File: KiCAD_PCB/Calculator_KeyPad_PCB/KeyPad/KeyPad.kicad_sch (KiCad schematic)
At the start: 42 parts

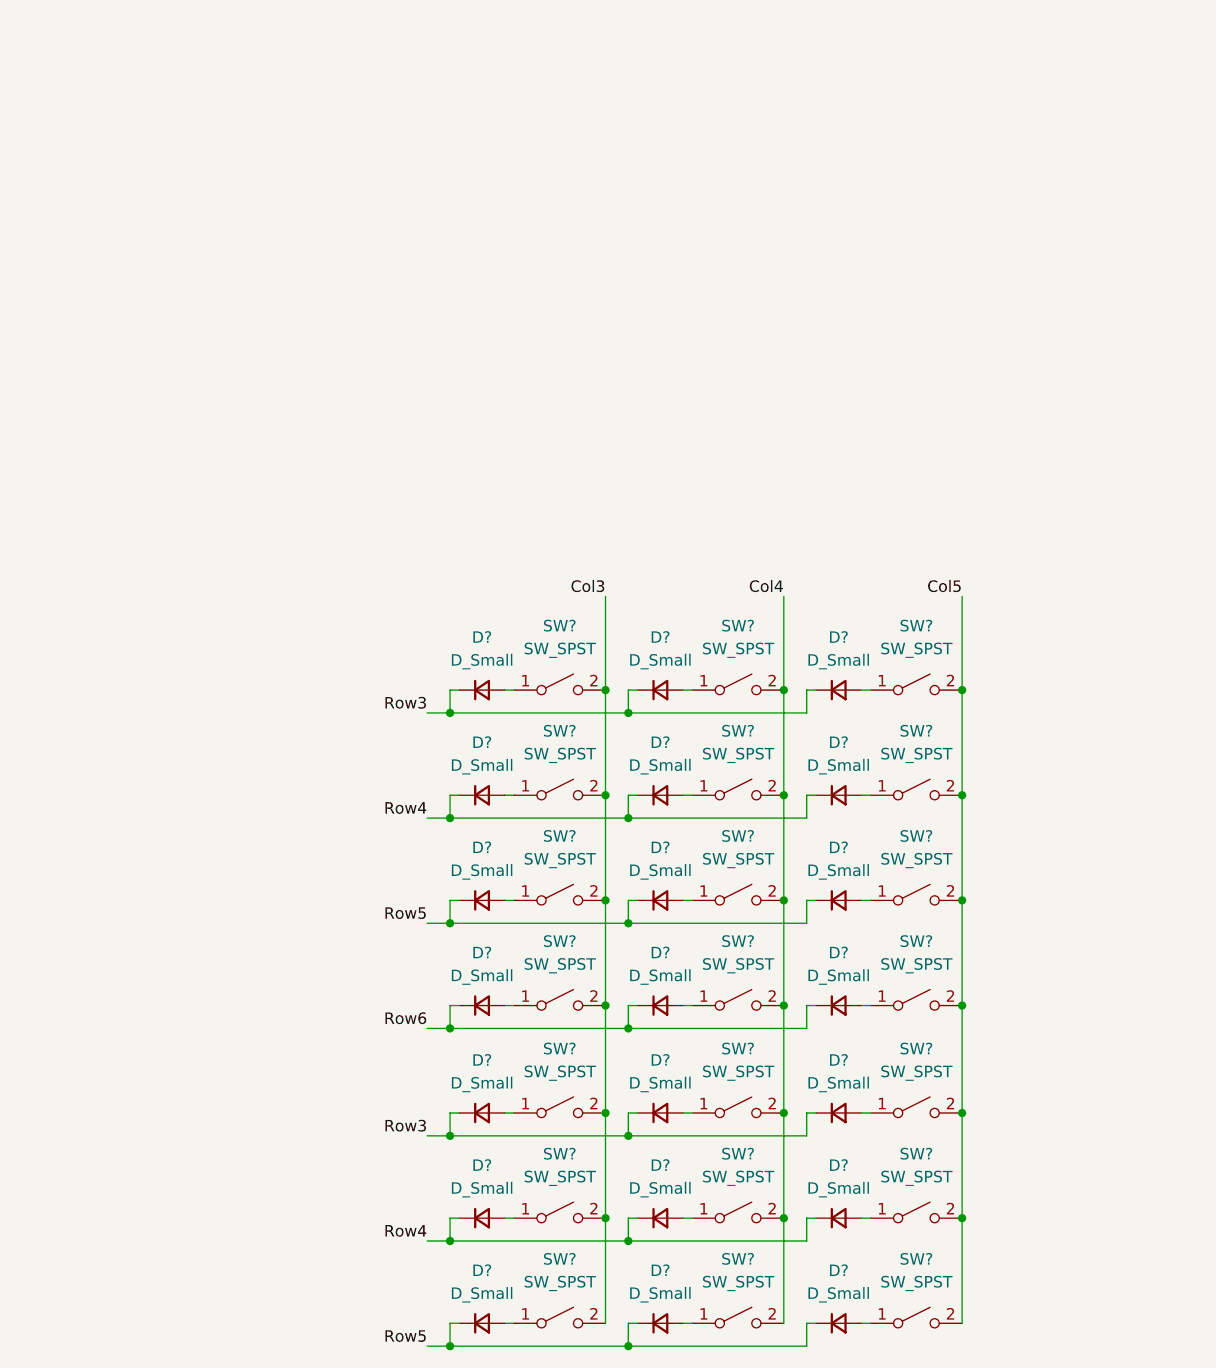
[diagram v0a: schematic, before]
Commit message: Updated NumberPad Schematic
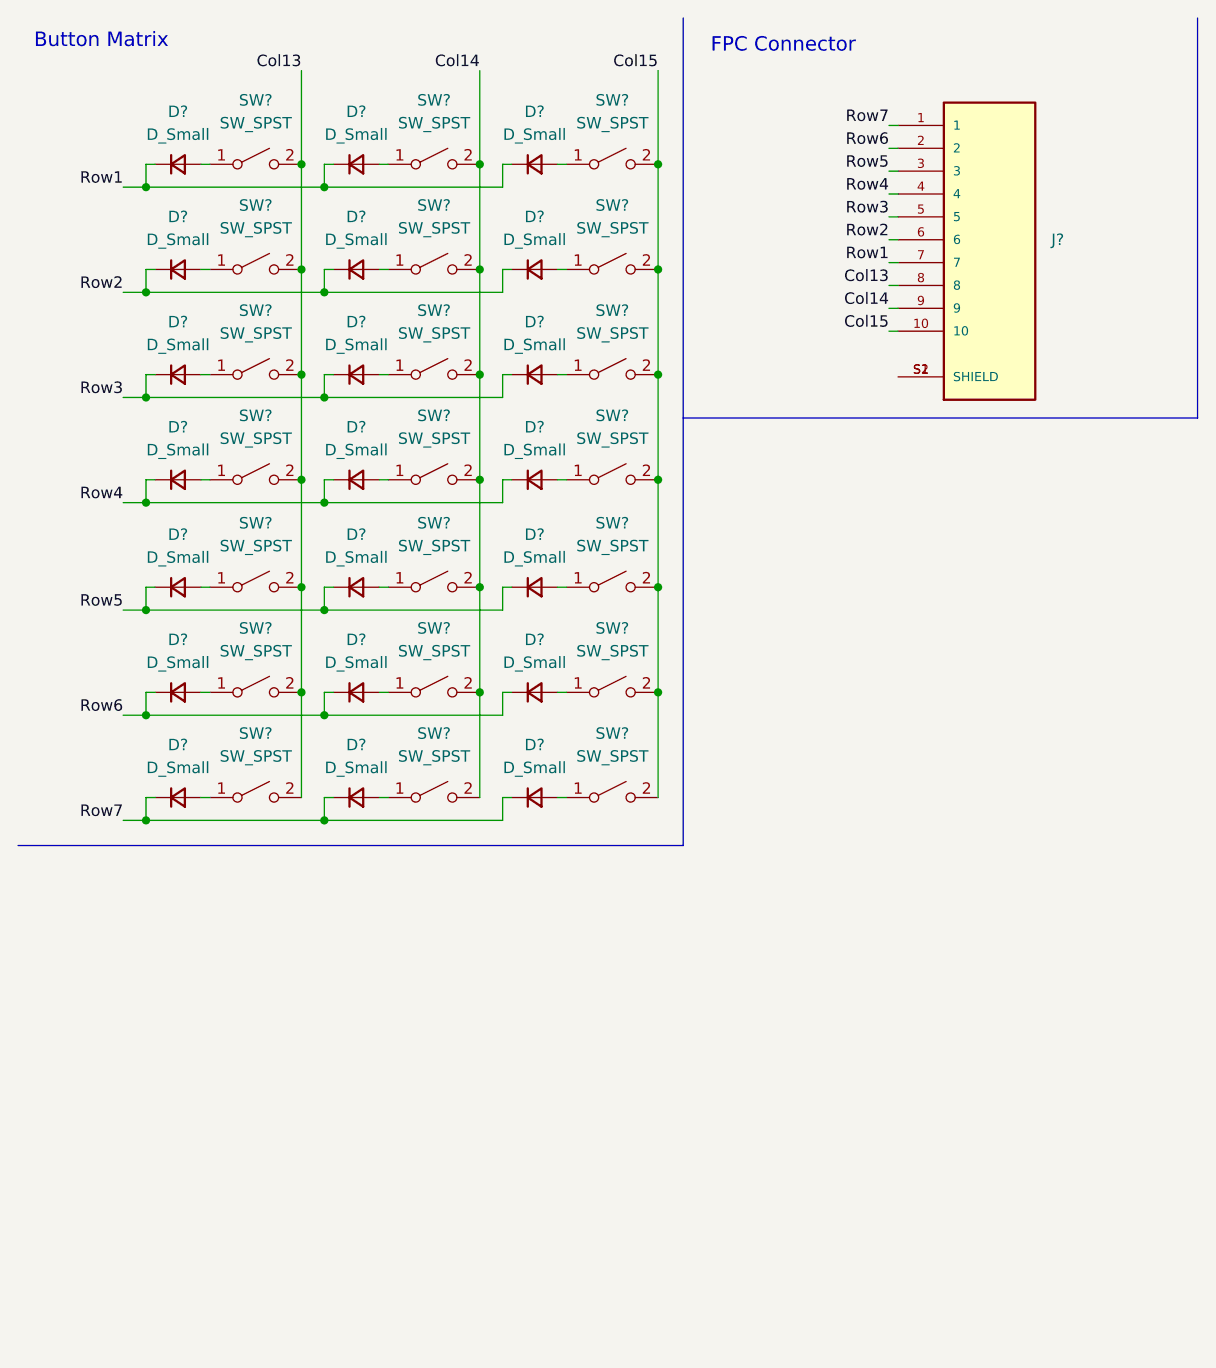
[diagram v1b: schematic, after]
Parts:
- added J?: (no value), symbol 5034801000:5034801000
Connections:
- net Row3: now also D?.1 (K), D?.1 (K), D?.1 (K), J?.5; no longer D?.1 (K), D?.1 (K), D?.1 (K), D?.1 (K), D?.1 (K), D?.1 (K)
- net Row4: now also D?.1 (K), D?.1 (K), D?.1 (K), J?.4; no longer D?.1 (K), D?.1 (K), D?.1 (K), D?.1 (K), D?.1 (K), D?.1 (K)
- net Row5: now also D?.1 (K), D?.1 (K), D?.1 (K), J?.3; no longer D?.1 (K), D?.1 (K), D?.1 (K), D?.1 (K), D?.1 (K), D?.1 (K)
- net Row6: now also D?.1 (K), D?.1 (K), D?.1 (K), J?.2; no longer D?.1 (K), D?.1 (K), D?.1 (K)
- net Col3 renamed Col13
- net Col13: now also J?.8
- net Col4 renamed Col14
- net Col14: now also J?.9
- net Col5 renamed Col15
- net Col15: now also J?.10
- new net: J?.S1 (SHIELD), J?.S2 (SHIELD)
- new net Row1: D?.1 (K), D?.1 (K), D?.1 (K), J?.7
- new net Row2: D?.1 (K), D?.1 (K), D?.1 (K), J?.6
- new net Row7: D?.1 (K), D?.1 (K), D?.1 (K), J?.1
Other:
- note added: "Button Matrix"
- note added: "FPC Connector"
- title: (none) -> Calculator Number Pad Module
- moved on the sheet: D?, SW?

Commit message: Finished NumPad Schematic
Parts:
- gave numbers to parts that had none: 43

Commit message: Working on PCB
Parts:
- SW1, SW10, SW11, SW12, SW13, SW14, SW15, SW16, SW17, SW18, SW19, SW2, SW20, SW21, SW3, SW4, SW5, SW6, SW7, SW8, SW9: footprint KSA1M331LFT_Footprint:KSA1M331LFT -> (none)

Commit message: NumPad Updates
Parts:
- J1: value (none) -> 5034801000; footprint (none) -> 5034801000:MOLEX_5034801000
- SW1, SW10, SW11, SW12, SW13, SW14, SW15, SW16, SW17, SW18, SW19, SW2, SW20, SW21, SW3, SW4, SW5, SW6, SW7, SW8, SW9: footprint (none) -> KSA_Switch:KSA1M331LFT
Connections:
- net Col13: now also J1.3; no longer J1.8
- net Col14: now also J1.2; no longer J1.9
- net Col15: now also J1.1; no longer J1.10
- net Row1: now also J1.4; no longer J1.7
- net Row2: now also J1.5; no longer J1.6
- net Row3: now also J1.6; no longer J1.5
- net Row4: now also J1.7; no longer J1.4
- net Row5: now also J1.8; no longer J1.3
- net Row6: now also J1.9; no longer J1.2
- net Row7: now also J1.10; no longer J1.1
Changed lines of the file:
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@@
     (effects (font (size 1.6 1.6)) (justify left bottom))
   )
-  (label "Row6" (at 108.712 26.67 180)
-    (effects (font (size 1.27 1.27)) (justify right bottom))
-  )
-  (label "Col13" (at 108.712 41.91 180)
+  (label "Row6" (at 108.712 44.45 180)
+    (effects (font (size 1.27 1.27)) (justify right bottom))
+  )
+  (label "Col13" (at 108.712 29.21 180)
     (effects (font (size 1.27 1.27)) (justify right bottom))
   )
@@
     (effects (font (size 1.27 1.27)) (justify right bottom))
   )
-  (label "Row4" (at 108.712 31.75 180)
-    (effects (font (size 1.27 1.27)) (justify right bottom))
-  )
-  (label "Row2" (at 108.712 36.83 180)
-    (effects (font (size 1.27 1.27)) (justify right bottom))
-  )
-  (label "Col15" (at 108.712 46.99 180)
+  (label "Row4" (at 108.712 39.37 180)
+    (effects (font (size 1.27 1.27)) (justify right bottom))
+  )
+  (label "Row2" (at 108.712 34.29 180)
+    (effects (font (size 1.27 1.27)) (justify right bottom))
+  )
+  (label "Col15" (at 108.712 24.13 180)
     (effects (font (size 1.27 1.27)) (justify right bottom))
   )
@@
     (effects (font (size 1.27 1.27)) (justify right bottom))
   )
-  (label "Row1" (at 108.712 39.37 180)
-    (effects (font (size 1.27 1.27)) (justify right bottom))
-  )
-  (label "Col14" (at 108.712 44.45 180)
+  (label "Row1" (at 108.712 31.75 180)
+    (effects (font (size 1.27 1.27)) (justify right bottom))
+  )
+  (label "Col14" (at 108.712 26.67 180)
     (effects (font (size 1.27 1.27)) (justify right bottom))
   )
@@
     (effects (font (size 1.27 1.27)) (justify right bottom))
   )
-  (label "Row3" (at 108.712 34.29 180)
-    (effects (font (size 1.27 1.27)) (justify right bottom))
-  )
-  (label "Row7" (at 108.712 24.13 180)
-    (effects (font (size 1.27 1.27)) (justify right bottom))
-  )
-  (label "Row5" (at 108.712 29.21 180)
+  (label "Row3" (at 108.712 36.83 180)
+    (effects (font (size 1.27 1.27)) (justify right bottom))
+  )
+  (label "Row7" (at 108.712 46.99 180)
+    (effects (font (size 1.27 1.27)) (justify right bottom))
+  )
+  (label "Row5" (at 108.712 41.91 180)
     (effects (font (size 1.27 1.27)) (justify right bottom))
   )
@@
     (property "Reference" "SW1" (id 0) (at 38.354 21.336 0))
     (property "Value" "SW_SPST" (id 1) (at 38.354 23.876 0))
-    (property "Footprint" "" (id 2) (at 38.354 28.448 0)
+    (property "Footprint" "KSA_Switch:KSA1M331LFT" (id 2) (at 38.354 28.448 0)
       (effects (font (size 1.27 1.27)) hide)
     )
@@
     (property "Reference" "SW5" (id 0) (at 38.354 68.326 0))
     (property "Value" "SW_SPST" (id 1) (at 38.354 70.866 0))
-    (property "Footprint" "" (id 2) (at 38.354 75.438 0)
+    (property "Footprint" "KSA_Switch:KSA1M331LFT" (id 2) (at 38.354 75.438 0)
       (effects (font (size 1.27 1.27)) hide)
     )
@@
     (property "Reference" "SW20" (id 0) (at 77.978 80.01 0))
     (property "Value" "SW_SPST" (id 1) (at 77.978 82.55 0))
-    (property "Footprint" "" (id 2) (at 77.978 87.122 0)
+    (property "Footprint" "KSA_Switch:KSA1M331LFT" (id 2) (at 77.978 87.122 0)
       (effects (font (size 1.27 1.27)) hide)
     )
@@
     (property "Reference" "SW6" (id 0) (at 38.354 80.01 0))
     (property "Value" "SW_SPST" (id 1) (at 38.354 82.55 0))
-    (property "Footprint" "" (id 2) (at 38.354 87.122 0)
+    (property "Footprint" "KSA_Switch:KSA1M331LFT" (id 2) (at 38.354 87.122 0)
       (effects (font (size 1.27 1.27)) hide)
     )
@@
     (property "Reference" "SW2" (id 0) (at 38.354 33.02 0))
     (property "Value" "SW_SPST" (id 1) (at 38.354 35.56 0))
-    (property "Footprint" "" (id 2) (at 38.354 40.132 0)
+    (property "Footprint" "KSA_Switch:KSA1M331LFT" (id 2) (at 38.354 40.132 0)
       (effects (font (size 1.27 1.27)) hide)
     )
@@
     (property "Reference" "SW3" (id 0) (at 38.354 44.704 0))
     (property "Value" "SW_SPST" (id 1) (at 38.354 47.244 0))
-    (property "Footprint" "" (id 2) (at 38.354 51.816 0)
+    (property "Footprint" "KSA_Switch:KSA1M331LFT" (id 2) (at 38.354 51.816 0)
       (effects (font (size 1.27 1.27)) hide)
     )
@@
       (effects (font (size 1.27 1.27)) (justify left))
     )
-    (property "Value" "" (id 1) (at 126.746 39.3699 0)
+    (property "Value" "5034801000" (id 1) (at 126.746 39.3699 0)
       (effects (font (size 1.27 1.27)) (justify left))
     )
-    (property "Footprint" "" (id 2) (at 119.888 39.37 0)
+    (property "Footprint" "5034801000:MOLEX_5034801000" (id 2) (at 119.888 39.37 0)
       (effects (font (size 1.27 1.27)) (justify left bottom) hide)
     )
@@
     (property "Reference" "SW21" (id 0) (at 77.978 91.694 0))
     (property "Value" "SW_SPST" (id 1) (at 77.978 94.234 0))
-    (property "Footprint" "" (id 2) (at 77.978 98.806 0)
+    (property "Footprint" "KSA_Switch:KSA1M331LFT" (id 2) (at 77.978 98.806 0)
       (effects (font (size 1.27 1.27)) hide)
     )
@@
     (property "Reference" "SW16" (id 0) (at 77.978 33.02 0))
     (property "Value" "SW_SPST" (id 1) (at 77.978 35.56 0))
-    (property "Footprint" "" (id 2) (at 77.978 40.132 0)
+    (property "Footprint" "KSA_Switch:KSA1M331LFT" (id 2) (at 77.978 40.132 0)
       (effects (font (size 1.27 1.27)) hide)
     )
@@
     (property "Reference" "SW19" (id 0) (at 77.978 68.326 0))
     (property "Value" "SW_SPST" (id 1) (at 77.978 70.866 0))
-    (property "Footprint" "" (id 2) (at 77.978 75.438 0)
+    (property "Footprint" "KSA_Switch:KSA1M331LFT" (id 2) (at 77.978 75.438 0)
       (effects (font (size 1.27 1.27)) hide)
     )
@@
     (property "Reference" "SW7" (id 0) (at 38.354 91.694 0))
     (property "Value" "SW_SPST" (id 1) (at 38.354 94.234 0))
-    (property "Footprint" "" (id 2) (at 38.354 98.806 0)
+    (property "Footprint" "KSA_Switch:KSA1M331LFT" (id 2) (at 38.354 98.806 0)
       (effects (font (size 1.27 1.27)) hide)
     )
@@
     (property "Reference" "SW9" (id 0) (at 58.166 33.02 0))
     (property "Value" "SW_SPST" (id 1) (at 58.166 35.56 0))
-    (property "Footprint" "" (id 2) (at 58.166 40.132 0)
+    (property "Footprint" "KSA_Switch:KSA1M331LFT" (id 2) (at 58.166 40.132 0)
       (effects (font (size 1.27 1.27)) hide)
     )
@@
     (property "Reference" "SW14" (id 0) (at 58.166 91.694 0))
     (property "Value" "SW_SPST" (id 1) (at 58.166 94.234 0))
-    (property "Footprint" "" (id 2) (at 58.166 98.806 0)
+    (property "Footprint" "KSA_Switch:KSA1M331LFT" (id 2) (at 58.166 98.806 0)
       (effects (font (size 1.27 1.27)) hide)
     )
@@
     (property "Reference" "SW8" (id 0) (at 58.166 21.336 0))
     (property "Value" "SW_SPST" (id 1) (at 58.166 23.876 0))
-    (property "Footprint" "" (id 2) (at 58.166 28.448 0)
+    (property "Footprint" "KSA_Switch:KSA1M331LFT" (id 2) (at 58.166 28.448 0)
       (effects (font (size 1.27 1.27)) hide)
     )
@@
     (property "Reference" "SW17" (id 0) (at 77.978 44.704 0))
     (property "Value" "SW_SPST" (id 1) (at 77.978 47.244 0))
-    (property "Footprint" "" (id 2) (at 77.978 51.816 0)
+    (property "Footprint" "KSA_Switch:KSA1M331LFT" (id 2) (at 77.978 51.816 0)
       (effects (font (size 1.27 1.27)) hide)
     )
@@
     (property "Reference" "SW10" (id 0) (at 58.166 44.704 0))
     (property "Value" "SW_SPST" (id 1) (at 58.166 47.244 0))
-    (property "Footprint" "" (id 2) (at 58.166 51.816 0)
+    (property "Footprint" "KSA_Switch:KSA1M331LFT" (id 2) (at 58.166 51.816 0)
       (effects (font (size 1.27 1.27)) hide)
     )
@@
     (property "Reference" "SW13" (id 0) (at 58.166 80.01 0))
     (property "Value" "SW_SPST" (id 1) (at 58.166 82.55 0))
-    (property "Footprint" "" (id 2) (at 58.166 87.122 0)
+    (property "Footprint" "KSA_Switch:KSA1M331LFT" (id 2) (at 58.166 87.122 0)
       (effects (font (size 1.27 1.27)) hide)
     )
@@
     (property "Reference" "SW15" (id 0) (at 77.978 21.336 0))
     (property "Value" "SW_SPST" (id 1) (at 77.978 23.876 0))
-    (property "Footprint" "" (id 2) (at 77.978 28.448 0)
+    (property "Footprint" "KSA_Switch:KSA1M331LFT" (id 2) (at 77.978 28.448 0)
       (effects (font (size 1.27 1.27)) hide)
     )
@@
     (property "Reference" "SW12" (id 0) (at 58.166 68.326 0))
     (property "Value" "SW_SPST" (id 1) (at 58.166 70.866 0))
-    (property "Footprint" "" (id 2) (at 58.166 75.438 0)
+    (property "Footprint" "KSA_Switch:KSA1M331LFT" (id 2) (at 58.166 75.438 0)
       (effects (font (size 1.27 1.27)) hide)
     )
@@
     (property "Reference" "SW18" (id 0) (at 77.978 56.388 0))
     (property "Value" "SW_SPST" (id 1) (at 77.978 58.928 0))
-    (property "Footprint" "" (id 2) (at 77.978 63.5 0)
+    (property "Footprint" "KSA_Switch:KSA1M331LFT" (id 2) (at 77.978 63.5 0)
       (effects (font (size 1.27 1.27)) hide)
     )
@@
     (property "Reference" "SW4" (id 0) (at 38.354 56.388 0))
     (property "Value" "SW_SPST" (id 1) (at 38.354 58.928 0))
-    (property "Footprint" "" (id 2) (at 38.354 63.5 0)
+    (property "Footprint" "KSA_Switch:KSA1M331LFT" (id 2) (at 38.354 63.5 0)
       (effects (font (size 1.27 1.27)) hide)
     )
@@
     (property "Reference" "SW11" (id 0) (at 58.166 56.388 0))
     (property "Value" "SW_SPST" (id 1) (at 58.166 58.928 0))
-    (property "Footprint" "" (id 2) (at 58.166 63.5 0)
-      (effects (font (size 1.27 1.27)) hide)
-    )
+    (property "Footprint" "KSA_Switch:KSA1M331LFT" (id 2) (at 58.166 63.5 0)
+      (effects (font (size 1.27 1.27)) hide)
+    )

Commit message: V2 Updates
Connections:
- net Col13: now also J1.8; no longer J1.3
- net Col14: now also J1.9; no longer J1.2
- net Col15: now also J1.10; no longer J1.1
- net Row1: now also J1.7; no longer J1.4
- net Row2: now also J1.6; no longer J1.5
- net Row3: now also J1.5; no longer J1.6
- net Row4: now also J1.4; no longer J1.7
- net Row5: now also J1.3; no longer J1.8
- net Row6: now also J1.2; no longer J1.9
- net Row7: now also J1.1; no longer J1.10
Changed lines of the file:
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@@
     (effects (font (size 1.6 1.6)) (justify left bottom))
   )
-  (label "Row6" (at 108.712 44.45 180)
+  (label "Row6" (at 108.712 26.67 180)
     (effects (font (size 1.27 1.27)) (justify right bottom))
   )
-  (label "Col13" (at 108.712 29.21 180)
+  (label "Col13" (at 108.712 41.91 180)
     (effects (font (size 1.27 1.27)) (justify right bottom))
   )
@@
     (effects (font (size 1.27 1.27)) (justify right bottom))
   )
-  (label "Row4" (at 108.712 39.37 180)
+  (label "Row4" (at 108.712 31.75 180)
     (effects (font (size 1.27 1.27)) (justify right bottom))
   )
-  (label "Row2" (at 108.712 34.29 180)
+  (label "Row2" (at 108.712 36.83 180)
     (effects (font (size 1.27 1.27)) (justify right bottom))
   )
-  (label "Col15" (at 108.712 24.13 180)
+  (label "Col15" (at 108.712 46.99 180)
     (effects (font (size 1.27 1.27)) (justify right bottom))
   )
@@
     (effects (font (size 1.27 1.27)) (justify right bottom))
   )
-  (label "Row1" (at 108.712 31.75 180)
+  (label "Row1" (at 108.712 39.37 180)
     (effects (font (size 1.27 1.27)) (justify right bottom))
   )
-  (label "Col14" (at 108.712 26.67 180)
+  (label "Col14" (at 108.712 44.45 180)
     (effects (font (size 1.27 1.27)) (justify right bottom))
   )
@@
     (effects (font (size 1.27 1.27)) (justify right bottom))
   )
-  (label "Row3" (at 108.712 36.83 180)
+  (label "Row3" (at 108.712 34.29 180)
     (effects (font (size 1.27 1.27)) (justify right bottom))
   )
-  (label "Row7" (at 108.712 46.99 180)
+  (label "Row7" (at 108.712 24.13 180)
     (effects (font (size 1.27 1.27)) (justify right bottom))
   )
-  (label "Row5" (at 108.712 41.91 180)
+  (label "Row5" (at 108.712 29.21 180)
     (effects (font (size 1.27 1.27)) (justify right bottom))
   )
